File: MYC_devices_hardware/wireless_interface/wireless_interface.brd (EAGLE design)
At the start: 62.2 x 47.9 mm, 43 parts, among them IC1 ATMEGA644A, IC2 7805DT, IC3 PCA9517, IC4 MAX3232CSE, Q1 20MH

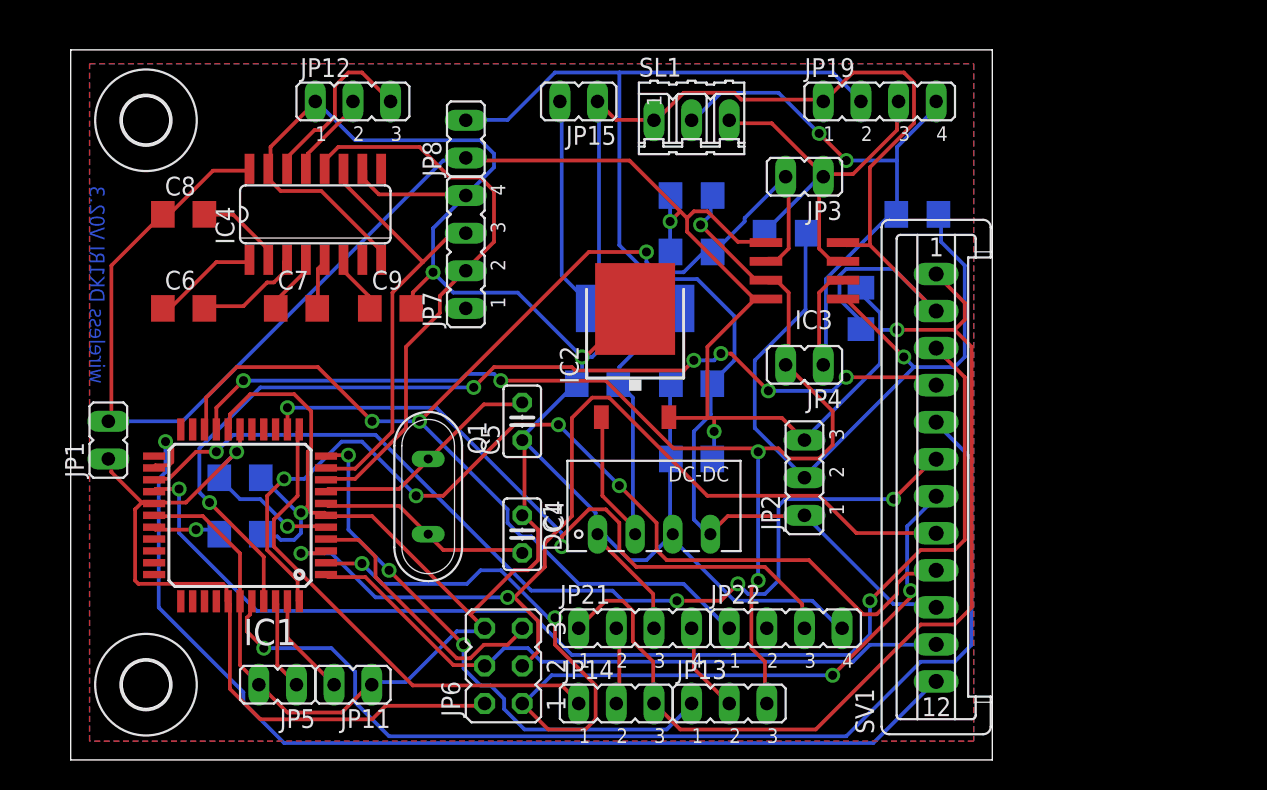
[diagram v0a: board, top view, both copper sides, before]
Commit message: new bord and firmware with Lora and 2.4GHz
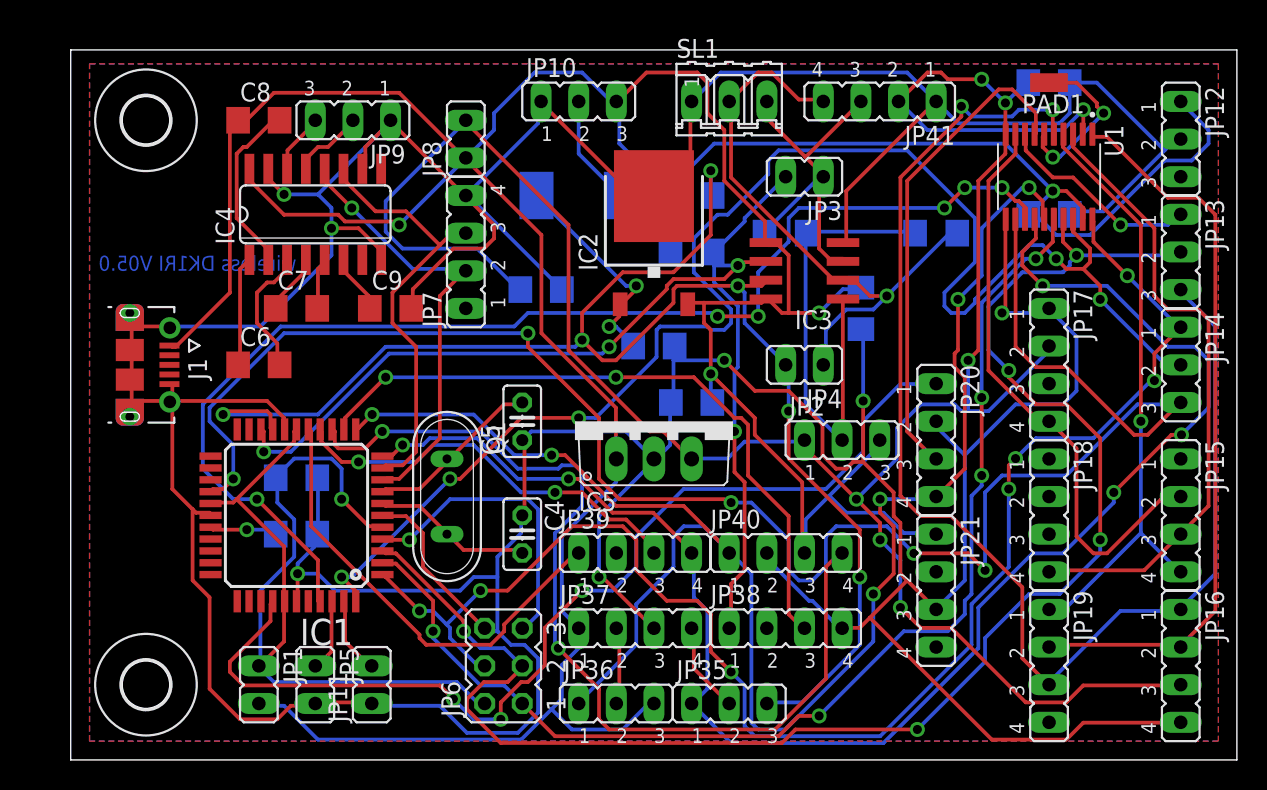
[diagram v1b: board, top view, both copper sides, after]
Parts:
- removed DC1: 12V - 3V, dc-dc-converter:NME
- removed SV1: wireless modul, con-amp-mt:S12P
- added C13, C14: 22uF, rcl:C1206
- added IC5: 7803, linear:TO220V
- added J1: 1050171001, 1050171001:MOLEX_1050171001
- added JP10: Power, jumper:JP2
- added JP16: nRF24L1 WLAN, jumper:JP4
- added JP17, JP18: nRF24L1s, jumper:JP4
- added JP20: Bluetooth, jumper:JP4
- added JP35: JP35, jumper:JP2
- added JP36: JP36, jumper:JP2
- added JP37: Sensor, jumper:JP4
- added JP39, JP40: GPS, jumper:JP4
- added JP41: Light Klima, jumper:JP4
- added JP9: RS232, jumper:JP2
- added PAD1: Pad1, wirepad:SMD1,27-2,54
- added U1: TXS0108EPWRG4, TXS0108EPWRG4:SOP65P640X120-20N
- JP12: value RS232 -> RFM95
- JP13: value JP13 -> RFM95
- JP14: value JP14 -> RFM95
- JP15: value 9-12V -> nRF24L1WLAN; device jumper:JP1 -> jumper:JP4
- JP19: value Light Klima -> nRF24L1s
- JP21: value Sensor -> Bluetooth
- moved JP12 55.9 mm to (74.9, 41.9), turned to 270 degrees
- moved JP15 49.3 mm to (74.9, 16.5), turned to 270 degrees
- moved JP14 44.4 mm to (74.9, 26.7), turned to 270 degrees
- moved JP13 43.1 mm to (74.9, 34.3), turned to 270 degrees
- moved JP19 39.8 mm to (66.0, 6.35), turned to 270 degrees
- moved JP21 20.5 mm to (58.4, 11.4), turned to 270 degrees
- moved JP1 19.4 mm to (12.7, 5.08), turned to 180 degrees
- moved C11 12.0 mm to (31.8, 31.8), turned to 180 degrees
- moved D1 8.52 mm to (34.3, 38.1), turned to 180 degrees
- moved C8 8.13 mm to (12.7, 43.2)
- moved IC2 7.73 mm to (39.4, 35.6)
- moved C6 6.35 mm to (12.7, 26.7)
- moved C1 4.58 mm to (39.4, 27.9), turned to 180 degrees
- moved C10 3.81 mm to (15.2, 19.1)
- moved C3 3.81 mm to (15.2, 15.2)
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- renumbered JP22 to JP38
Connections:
- removed net N$31: D1.A, JP15.2
- removed net RESET_W: IC1.26, SV1.3
- removed net X1: IC1.41, SV1.4
- removed net X2: IC1.40, SV1.5
- removed net X3: IC1.25, SV1.6
- removed net X4: IC1.24, SV1.12
- new net B_MOD: IC1.37, JP20.1
- new net COM2_RX*: JP20.3, U1.7
- new net COM2_TX_50HZ*: PAD1.1, U1.6
- new net GEN: IC1.16, JP39.1
- new net GFIX: IC1.15, JP39.3
- new net GPPS: IC1.14, JP40.4
- new net INT/G0*: JP13.1, U1.8
- new net INT_G0: IC1.41, U1.13
- new net MISO: IC1.2, JP6.1, U1.16
- new net MOSI: IC1.1, JP14.1, JP6.4, U1.20
- new net N$11: D1.A, JP10.2
- new net RESET/CE*: JP15.2, JP17.4, U1.9
- new net RESET_CE: IC1.26, JP14.3, U1.12
- new net SCK: IC1.3, JP13.2, JP6.3, U1.17
- new net SCS: IC1.44, JP14.2, U1.18
- net COM2_RX: now also JP35.1, JP39.4, U1.14; no longer JP13.1
- net COM2_TX/50HZ: now also JP20.4, JP36.1, JP40.1, U1.15; no longer JP14.1
- net GND: now also C13.2, C14.2, IC5.2, J1.5, J1.SH1, J1.SH2, J1.SH3, J1.SH4, J1.SH5, J1.SH6, JP10.1, JP12.2, JP16.4, JP17.1, JP20.2, JP37.3, JP40.2, JP41.1, JP9.1, U1.11; no longer DC1.1, DC1.3, JP12.1, JP15.1, JP19.1, SV1.2
- net MISO*: now also JP13.3, JP16.1, JP19.3, U1.5; no longer IC1.2, JP6.1, SV1.7
- net MOSI*: now also JP16.2, JP19.2, U1.1; no longer IC1.1, JP6.4, SV1.11
- net N$1: now also JP36.2, JP37.2; no longer JP14.2, JP21.2
- net N$16: now also JP9.3; no longer JP12.3
- net N$17: now also JP35.2, JP37.4; no longer JP13.2, JP21.4
- net N$3: now also JP9.2; no longer JP12.2
- net N$35: no longer DC1.2
- net SCK*: now also JP15.4, JP19.1, U1.4; no longer IC1.3, JP6.3, SV1.8
- net SCL: now also JP35.3; no longer JP13.3
- net SCL_IN: now also JP41.4; no longer JP19.4
- net SCS*: now also JP15.3, JP18.4, U1.3; no longer IC1.44, SV1.9
- net SDA_IN: now also JP41.3; no longer JP19.3
- net VCC: now also C13.1, IC5.1, J1.1, JP10.3, JP12.1, JP36.3, JP37.1, JP40.3, U1.19; no longer JP14.3, SV1.1
- net VDD: now also C14.1, IC5.3, JP16.3, JP17.2, JP41.2, U1.10, U1.2; no longer DC1.4, JP19.2, SV1.10
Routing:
- net GND: track 287.0 -> 427.6 mm, vias 3 -> 7
- net RESET_CE: track 0.00 -> 120.9 mm, vias 0 -> 5
- net SCK: track 0.00 -> 106.8 mm, vias 0 -> 5
- net MOSI: track 0.00 -> 100.2 mm, vias 0 -> 7
- net SCS: track 0.00 -> 100.1 mm, vias 0 -> 5
- net VCC: track 192.1 -> 285.6 mm, vias 3 -> 4
- net INT_G0: track 0.00 -> 83.4 mm, vias 0 -> 6
- net RESET_W: track 79.5 -> 0.00 mm, vias 2 -> 0
- net COM2_TX/50HZ: track 33.6 -> 112.6 mm, vias 0 -> 6
- net MISO: track 0.00 -> 78.6 mm, vias 0 -> 5
- net VDD: track 85.0 -> 161.8 mm, vias 0 -> 7
- net X2: track 73.8 -> 0.00 mm, vias 1 -> 0
- net X4: track 72.8 -> 0.00 mm, vias 1 -> 0
- net B_MOD: track 0.00 -> 68.9 mm, vias 0 -> 3
- net COM2_RX: track 37.4 -> 105.1 mm, vias 3 -> 5
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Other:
- board size 62.2 x 47.9 mm -> 78.7 x 47.9 mm
- board text added: "wireless DK1RI V05.0"
- board text removed: "wireless DK1RI V02.3"
